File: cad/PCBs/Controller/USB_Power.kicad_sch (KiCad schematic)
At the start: 3 parts, among them U1 STUSB4500QTR

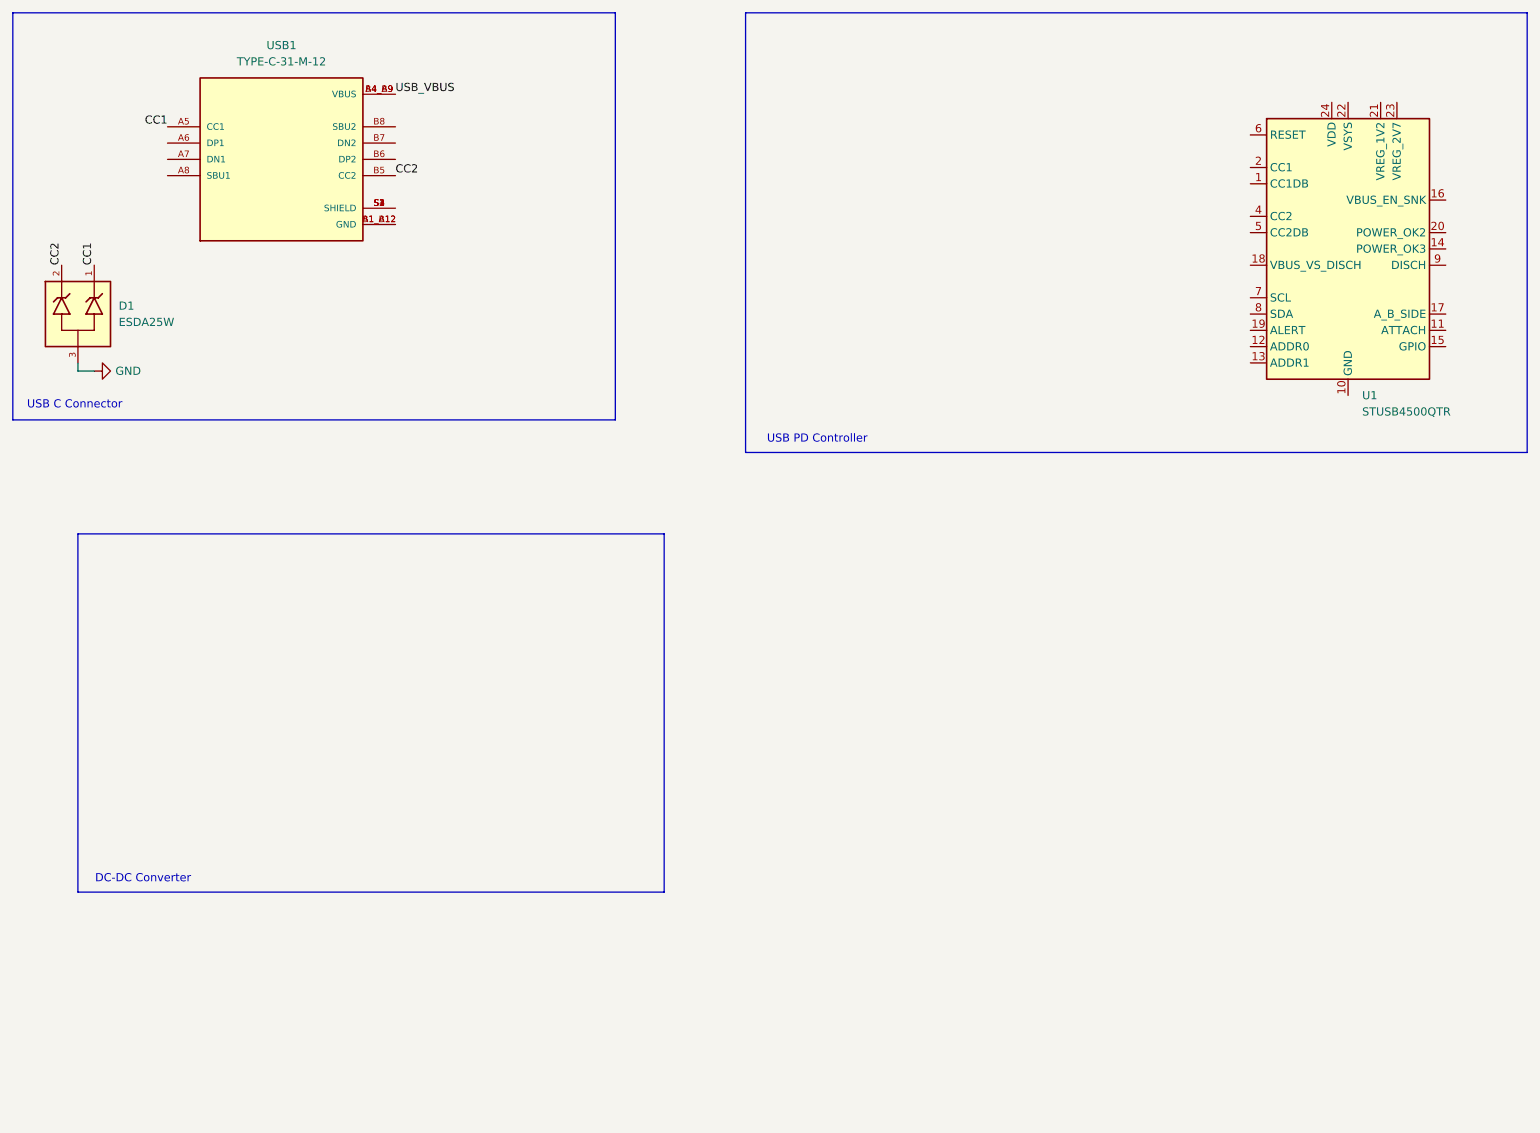
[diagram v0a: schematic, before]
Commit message: Finish schematic for PD Controller
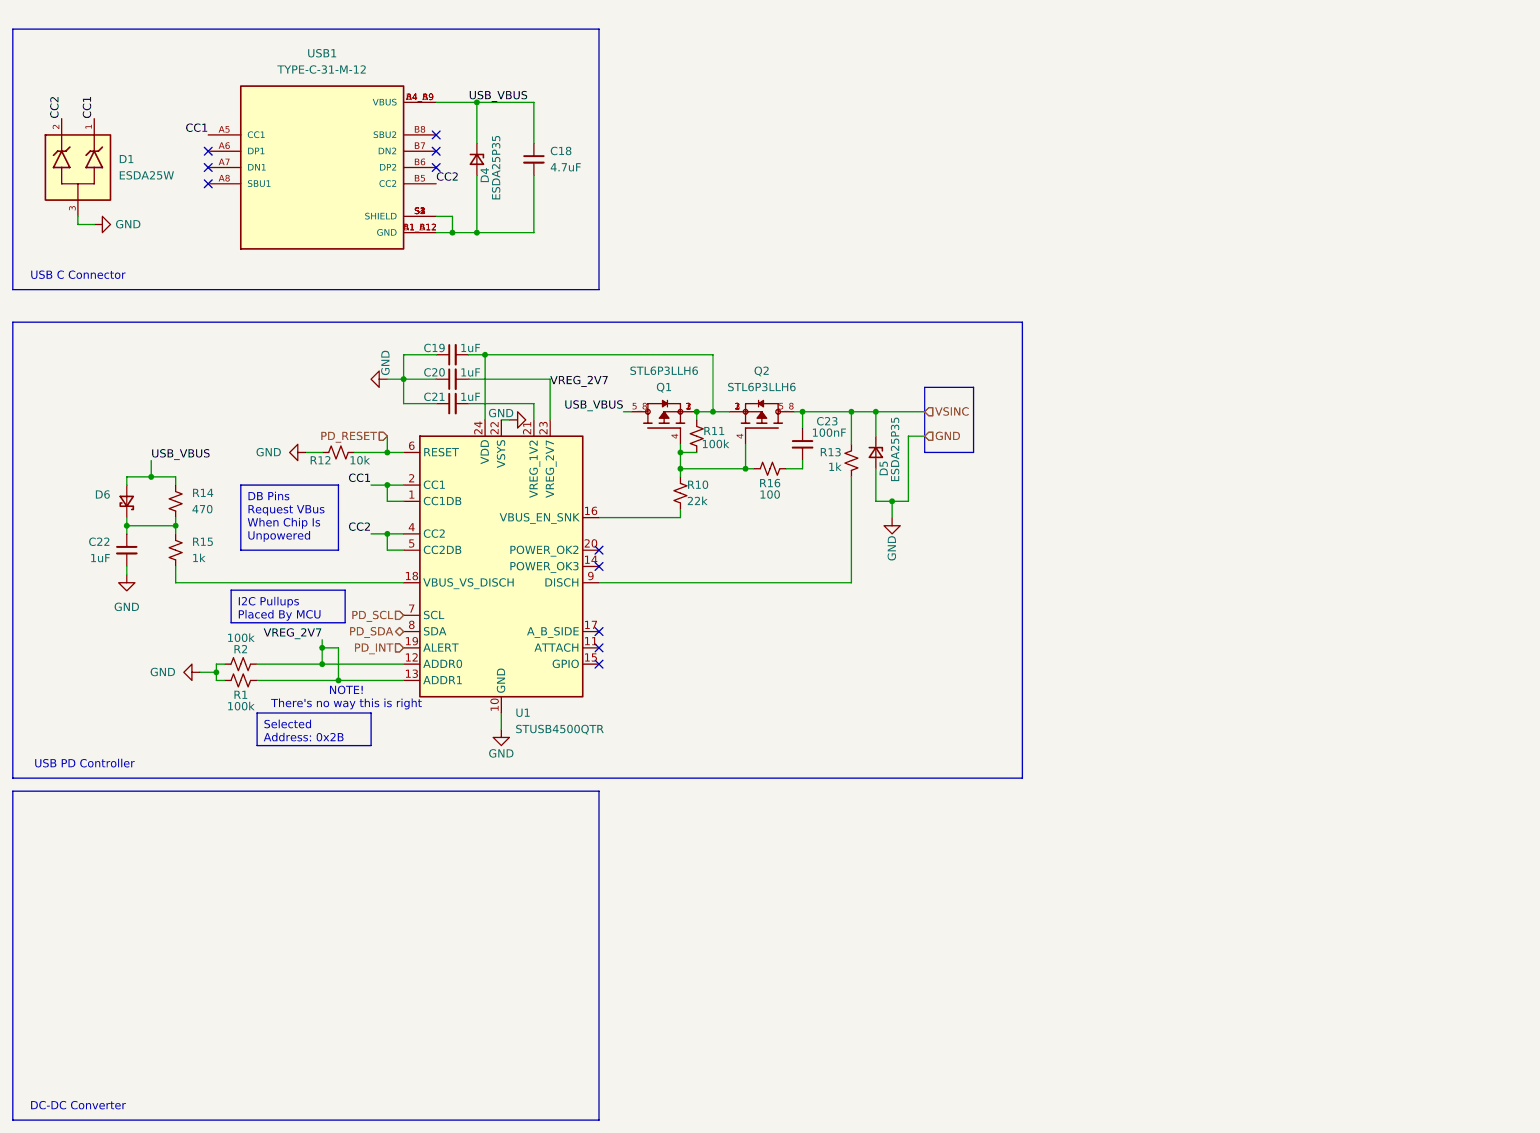
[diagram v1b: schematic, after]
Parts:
- added C18: 4.7uF, symbol Device:C_Small
- added C19, C20, C21, C22: 1uF, symbol Device:C_Small
- added C23: 100nF, symbol Device:C_Small
- added D4, D5: ESDA25P35, symbol Device:D_Zener_Small
- added D6: D_Schottky_Small, symbol Device:D_Schottky_Small
- added Q1, Q2: STL6P3LLH6, STL6P3LLH6:TRANS_STL6P3LLH6, symbol STL6P3LLH6:STL6P3LLH6
- added R1, R11, R2: 100k, symbol Device:R_Small_US
- added R10: 22k, symbol Device:R_Small_US
- added R12: 10k, symbol Device:R_Small_US
- added R13, R15: 1k, symbol Device:R_Small_US
- added R14: 470, symbol Device:R_Small_US
- added R16: 100, symbol Device:R_Small_US
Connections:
- net CC1: now also U1.1 (CC1DB), U1.2 (CC1)
- net CC2: now also U1.4 (CC2), U1.5 (CC2DB)
- net GND: now also U1.10 (GND), U1.22 (VSYS), U1.25 (GND), C19.1, C20.1, C21.1, C22.2, D5.2 (A), R1.2, R12.1, R2.1
- net USB_VBUS: now also C18.1, D4.1 (K), D6.2 (A), Q1.5_8, R14.1
- net at USB1.A1_B12 (GND), USB1.B1_A12 (GND): now also USB1.S1 (SHIELD), USB1.S2 (SHIELD), USB1.S3 (SHIELD), USB1.S4 (SHIELD), C18.2, D4.2 (A)
- net VREG_2V7: now reaches U1.12 (ADDR0)
- net VREG_2V7: now also U1.13 (ADDR1), U1.23 (VREG_2V7), C20.2, R1.1, R2.2
- net at U1.16 (VBUS_EN_SNK): now also R10.2
- net at U1.18 (VBUS_VS_DISCH): now also R15.2
- net PD_INT: now reaches U1.19 (ALERT)
- net at U1.21 (VREG_1V2): now also C21.2
- net at U1.24 (VDD): now also C19.2, Q1.1, Q1.2, Q1.3, Q2.1, Q2.2, Q2.3, R11.1
- net PD_RESET: now reaches U1.6 (RESET)
- net PD_RESET: now also R12.2
- net PD_SCL: now reaches U1.7 (SCL)
- net PD_SDA: now reaches U1.8 (SDA)
- net at U1.9 (DISCH): now also R13.2
- new net: C22.1, D6.1 (K), R14.2, R15.1
- new net: Q1.4, Q2.4, R10.1, R11.2, R16.1
- new net: C23.2, R16.2
- new net VSINC: C23.1, D5.1 (K), Q2.5_8, R13.1
- no-connect marks 0 -> 11
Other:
- note added: "NOTE! There's no way this is right"
- moved on the sheet: D1, U1, USB1
